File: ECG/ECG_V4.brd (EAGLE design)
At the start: 32 parts, among them U1 AD8232, U3 BGM111-VISUAL-A

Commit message: Added LED circuit
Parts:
- added D2: RED, SparkFun-LED:LED-0603
- added R39: 1k, SparkFun-Resistors:0603-RES
- added SJ1: LED DISABLE, SparkFun-Passives:SJ_2S-TRACE
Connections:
- new net N$36: D2.A, R39.1
- new net N$37: D2.C, SJ1.2
- new net N$38: R39.2
- net GND: now also SJ1.1
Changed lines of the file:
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@@
 <element name="JP1" library="LilyPad-Wearables" package="PETAL-LONG-2" value="SEWTAP2" x="13.716" y="31.623" rot="MR0"/>
 <element name="JP2" library="LilyPad-Wearables" package="PETAL-LONG-2" value="SEWTAP2" x="58.166" y="33.274" rot="MR0"/>
+<element name="R39" library="SparkFun-Resistors" package="0603-RES" value="1k" x="6.858" y="42.545">
+<attribute name="PROD_ID" value="RES-07856" x="6.858" y="46.609" size="1.778" layer="27" display="off"/>
+</element>
+<element name="D2" library="SparkFun-LED" package="LED-0603" value="RED" x="6.604" y="39.624">
+<attribute name="PROD_ID" value="DIO-00819" x="6.604" y="43.688" size="1.778" layer="27" display="off"/>
+</element>
+<element name="SJ1" library="SparkFun-Passives" package="SJ_2S-TRACE" value="LED DISABLE" x="6.731" y="46.101"/>
 </elements>
 <signals>
@@
 <wire x1="50.673" y1="38.1" x2="49.1998" y2="38.1" width="0.8128" layer="16"/>
 <wire x1="49.1998" y1="38.1" x2="49.1998" y2="37.4777" width="0.8128" layer="16"/>
+<contactref element="SJ1" pad="1"/>
 <wire x1="35.687" y1="47.035" x2="27.875" y2="48.433" width="0" layer="19" extent="1-16"/>
 <wire x1="16.575" y1="48.433" x2="27.875" y2="48.433" width="0" layer="19" extent="1-1"/>
+<wire x1="6.223" y1="46.101" x2="16.575" y2="48.433" width="0" layer="19" extent="1-1"/>
 <wire x1="27.875" y1="35.233" x2="27.875" y2="48.433" width="0" layer="19" extent="1-1"/>
 <wire x1="16.575" y1="35.233" x2="27.875" y2="35.233" width="0" layer="19" extent="1-1"/>
@@
 <wire x1="22.352" y1="21.082" x2="27.875" y2="37.633" width="0" layer="19" extent="1-1"/>
 </signal>
+<signal name="N$36">
+<contactref element="R39" pad="1"/>
+<contactref element="D2" pad="A"/>
+<wire x1="6.604" y1="38.874" x2="6.008" y2="42.545" width="0" layer="19" extent="1-1"/>
+</signal>
+<signal name="N$37">
+<contactref element="D2" pad="C"/>
+<contactref element="SJ1" pad="2"/>
+<wire x1="6.604" y1="40.374" x2="7.239" y2="46.101" width="0" layer="19" extent="1-1"/>
+</signal>
+<signal name="N$38">
+<contactref element="R39" pad="2"/>
+</signal>
 </signals>

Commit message: Completed Routing
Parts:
- moved LOGO1 44.7 mm to (57.0, 43.2)
- moved D2 9.31 mm to (15.9, 40.5)
- moved R39 9.31 mm to (16.1, 43.4)
- moved SJ1 9.31 mm to (16.0, 47.0)
- moved U3 4.70 mm to (26.9, 41.7)
- moved JP2 1.43 mm to (58.5, 31.9)
- moved BAT1 0.40 mm to (36.1, 32.5)
- moved C1 0.40 mm to (45.0, 25.1)
- moved C3 0.40 mm to (41.7, 27.6)
- moved C5 0.40 mm to (47.2, 34.7)
- moved C6 0.40 mm to (45.5, 41.8)
- moved C7 0.40 mm to (47.1, 37.3)
- moved J2 0.40 mm to (20.2, 20.6)
- moved R1 0.40 mm to (35.8, 34.7)
- moved R14 0.40 mm to (47.1, 38.9)
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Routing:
- net GND: track 54.9 -> 127.3 mm, vias 3 -> 5
- net N$29: track 0.67 -> 34.8 mm, vias 0 -> 2
- net N$31: track 0.00 -> 23.0 mm, vias 0 -> 2
- net N$33: track 0.00 -> 21.2 mm, vias 0 -> 2
- net N$37: track 0.00 -> 10.4 mm
- net 3.3V: track 64.5 -> 72.1 mm
- net N$36: track 0.00 -> 4.10 mm
- net RA: track 45.7 -> 44.6 mm
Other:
- board outline added: 62.2 x 34.3 mm

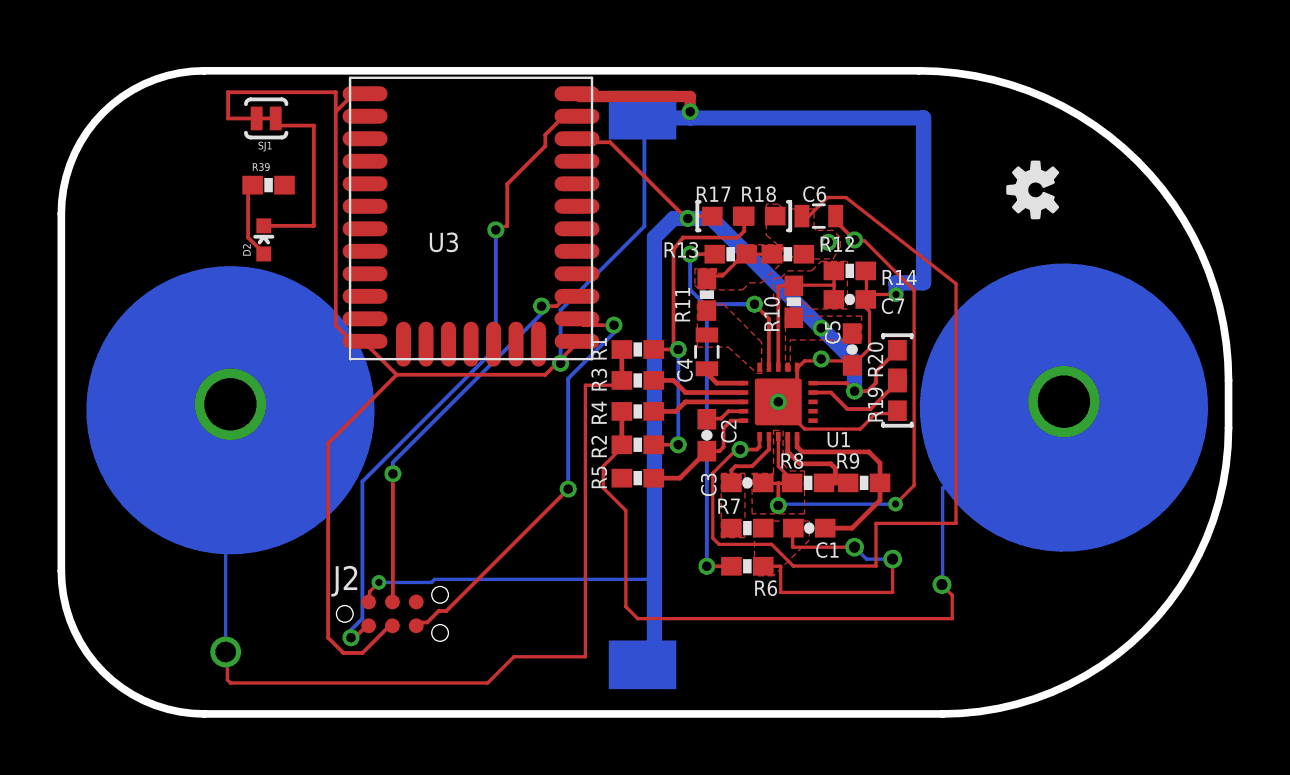
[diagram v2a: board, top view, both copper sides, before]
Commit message: Added Ground Plane
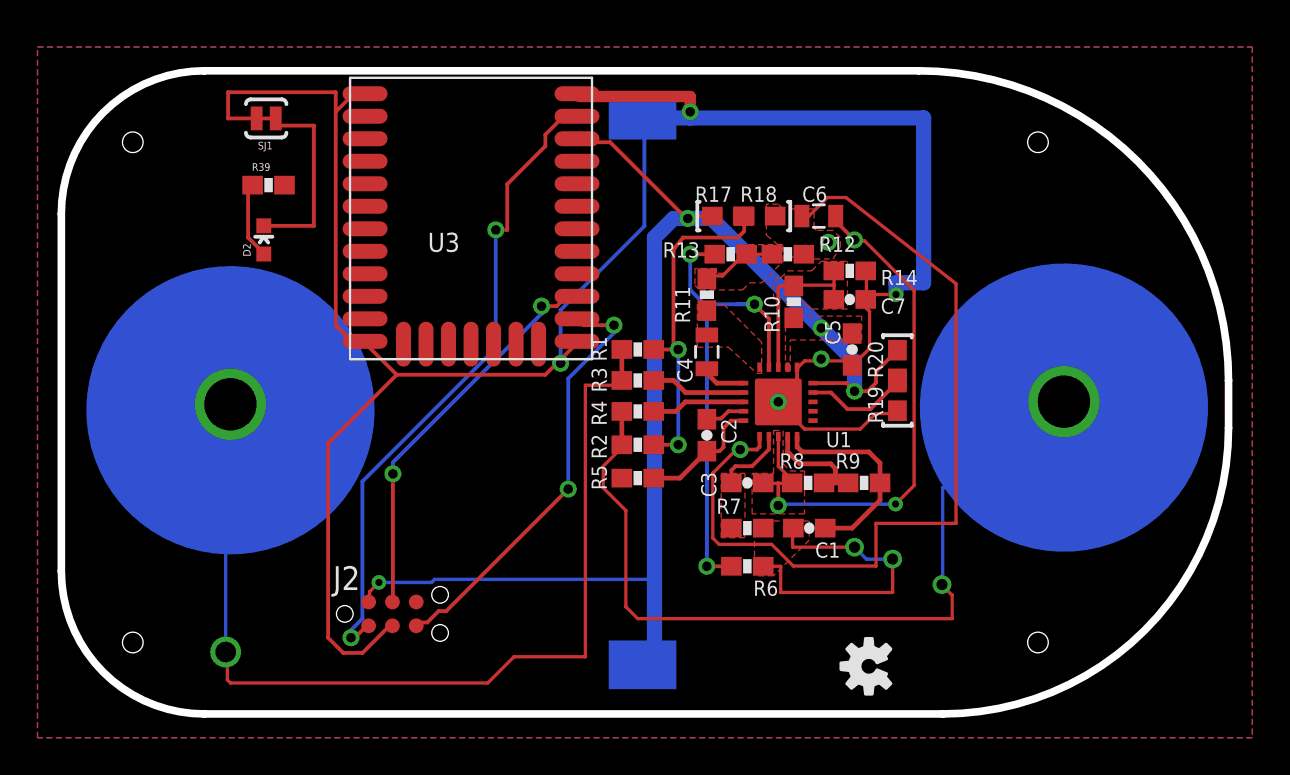
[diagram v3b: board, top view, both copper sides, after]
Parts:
- moved LOGO1 26.9 mm to (48.1, 17.8)
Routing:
- added copper zone on layer 1, net GND
- added copper zone on layer 16, net GND
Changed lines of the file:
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@@
 <setting verticaltext="up"/>
 </settings>
-<grid distance="0.005" unitdist="inch" unit="inch" style="lines" multiple="1" display="yes" altdistance="0.01" altunitdist="inch" altunit="inch"/>
+<grid distance="0.05" unitdist="inch" unit="inch" style="lines" multiple="1" display="yes" altdistance="0.01" altunitdist="inch" altunit="inch"/>
 <layers>
 <layer number="1" name="Top" color="4" fill="1" visible="yes" active="yes"/>
@@
 <layer number="25" name="tNames" color="7" fill="1" visible="yes" active="yes"/>
 <layer number="26" name="bNames" color="7" fill="1" visible="yes" active="yes"/>
-<layer number="27" name="tValues" color="7" fill="1" visible="no" active="yes"/>
-<layer number="28" name="bValues" color="7" fill="1" visible="no" active="yes"/>
-<layer number="29" name="tStop" color="7" fill="3" visible="no" active="yes"/>
-<layer number="30" name="bStop" color="7" fill="6" visible="no" active="yes"/>
-<layer number="31" name="tCream" color="7" fill="4" visible="no" active="yes"/>
-<layer number="32" name="bCream" color="7" fill="5" visible="no" active="yes"/>
-<layer number="33" name="tFinish" color="6" fill="3" visible="no" active="yes"/>
-<layer number="34" name="bFinish" color="6" fill="6" visible="no" active="yes"/>
-<layer number="35" name="tGlue" color="7" fill="4" visible="no" active="yes"/>
+<layer number="27" name="tValues" color="7" fill="1" visible="yes" active="yes"/>
+<layer number="28" name="bValues" color="7" fill="1" visible="yes" active="yes"/>
+<layer number="29" name="tStop" color="7" fill="3" visible="yes" active="yes"/>
+<layer number="30" name="bStop" color="7" fill="6" visible="yes" active="yes"/>
+<layer number="31" name="tCream" color="7" fill="4" visible="yes" active="yes"/>
+<layer number="32" name="bCream" color="7" fill="5" visible="yes" active="yes"/>
+<layer number="33" name="tFinish" color="6" fill="3" visible="yes" active="yes"/>
+<layer number="34" name="bFinish" color="6" fill="6" visible="yes" active="yes"/>
+<layer number="35" name="tGlue" color="7" fill="4" visible="yes" active="yes"/>
 <layer number="36" name="bGlue" color="7" fill="5" visible="yes" active="yes"/>
 <layer number="37" name="tTest" color="7" fill="1" visible="yes" active="yes"/>
@@
 <wire x1="52.07" y1="15.24" x2="67.31" y2="30.48" width="0.4064" layer="20" curve="90"/>
 <wire x1="67.31" y1="30.48" x2="67.31" y2="33.02" width="0.4064" layer="20"/>
+<hole x="8.89" y="19.05" drill="1.1"/>
+<hole x="8.89" y="45.72" drill="1.1"/>
+<hole x="57.15" y="45.72" drill="1.1"/>
+<hole x="57.15" y="19.05" drill="1.1"/>
 </plain>
 <attributes>
@@
 <attribute name="VALUE" x="36.83" y="28.956" size="0.4064" layer="27" font="vector" rot="R180"/>
 </element>
-<element name="LOGO1" library="SparkFun-Aesthetics" package="OSHW-LOGO-S" value="OSHW-LOGOS" x="57.023" y="43.18" rot="R90"/>
+<element name="LOGO1" library="SparkFun-Aesthetics" package="OSHW-LOGO-S" value="OSHW-LOGOS" x="48.133" y="17.78" rot="R90"/>
 <element name="R17" library="SparkFun-Resistors" package="0603" value="0" x="40.64" y="41.783" smashed="yes">
 <attribute name="PROD_ID" value="RES-08609" x="40.64" y="41.783" size="1.778" layer="27" display="off"/>
@@
 <wire x1="13.97" y1="48.387" x2="19.7104" y2="48.387" width="0.2032" layer="1"/>
 <wire x1="19.7104" y1="48.387" x2="19.7104" y2="47.3456" width="0.2032" layer="1"/>
+<polygon width="0.4064" layer="16">
+<vertex x="3.81" y="50.8"/>
+<vertex x="68.58" y="50.8"/>
+<vertex x="68.58" y="13.97"/>
+<vertex x="3.81" y="13.97"/>
+</polygon>
+<polygon width="0.4064" layer="1">
+<vertex x="3.81" y="50.8"/>
+<vertex x="68.58" y="50.8"/>
+<vertex x="68.58" y="13.97"/>
+<vertex x="3.81" y="13.97"/>
+</polygon>
 </signal>
 <signal name="N$1">
@@
 <contactref element="U3" pad="RESET"/>
 <contactref element="J2" pad="1"/>
-<wire x1="28.7782" y1="41.2369" x2="28.22849375" y2="41.1311875" width="0.1778" layer="1"/>
-<wire x1="28.22849375" y1="41.1311875" x2="28.1178" y2="41.1099" width="0.1778" layer="1"/>
-<wire x1="28.8544" y1="43.4848" x2="28.8544" y2="41.2496" width="0.2032" layer="1"/>
+<wire x1="28.8544" y1="43.4848" x2="28.8544" y2="41.0464" width="0.2032" layer="1"/>
 <wire x1="30.8864" y1="45.5168" x2="28.8544" y2="43.4848" width="0.2032" layer="1"/>
 <wire x1="30.8864" y1="46.1264" x2="30.8864" y2="45.5168" width="0.2032" layer="1"/>
 <wire x1="31.6992" y1="46.9392" x2="30.8864" y2="46.1264" width="0.2032" layer="1"/>
 <wire x1="32.512" y1="46.9392" x2="31.6992" y2="46.9392" width="0.2032" layer="1"/>
-<wire x1="28.8544" y1="41.2496" x2="28.7782" y2="41.2369" width="0.2032" layer="1"/>
 <wire x1="32.512" y1="46.9392" x2="32.574" y2="47.106" width="0.2032" layer="1"/>
 <wire x1="20.7264" y1="19.304" x2="21.336" y2="19.9136" width="0.2032" layer="1"/>
@@
 <wire x1="28.2448" y1="41.0464" x2="28.2448" y2="34.7472" width="0.2032" layer="16"/>
 <wire x1="21.336" y1="19.9136" x2="21.463" y2="19.939" width="0.2032" layer="1"/>
-<wire x1="28.2448" y1="41.0464" x2="28.22849375" y2="41.1311875" width="0.2032" layer="1"/>
 <via x="20.5232" y="19.304" extent="1-16" drill="0.508"/>
 <via x="28.2448" y="41.0464" extent="1-16" drill="0.508"/>
+<wire x1="28.2448" y1="41.0464" x2="28.8544" y2="41.0464" width="0.2032" layer="1"/>
 </signal>
 <signal name="N$31">
